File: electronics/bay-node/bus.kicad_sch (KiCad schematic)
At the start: 9 parts, among them U11 TCAN1044AV

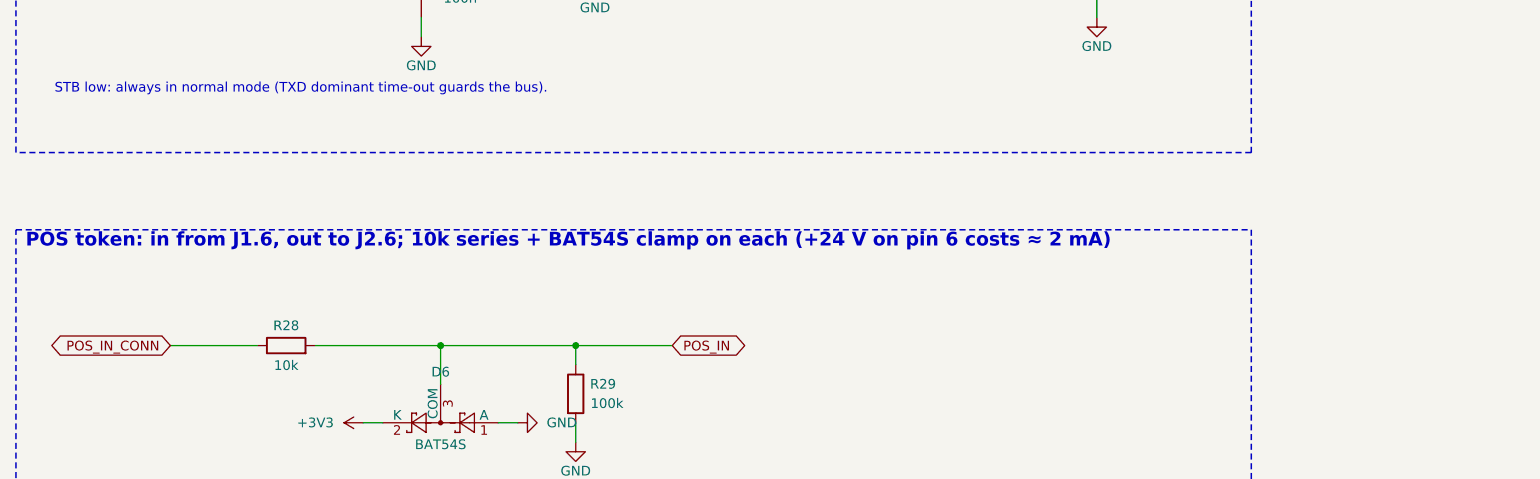
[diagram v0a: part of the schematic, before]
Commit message: Bay node v0.5: VRACK, GCT USB-C, VBUS caps on the ESD parts
Follows the power box's switch to USB-C PD (docs/can.md on the power-box branch):

- Pin 1 of the row cable is VRACK (20 V, or 28 V EPR): the net 24V_BUS becomes
  VRACK and +24V (after the P-FET) becomes VIN, in the schematic, the zones and
  the netclass patterns.  The input stage already takes 20-28 V.
- J3/J4 become the GCT USB4105-GF-A-120 (catalog usbc5a, LCSC C5184243), the
  part the user approved for the hub.  KiCad 10 ships its 3D model.  The pads
  sit 0.365 mm closer to the footprint origin than the HRO's, so the hand-drawn
  USB High-Speed tracks move with them (both lines of each pair alike, so the
  matching holds).  A board rule allows the footprint's own 0.19 mm between its
  GND pads and its pegs, the same rule the hub uses.
- Konnect's open point from v0.4: C25 and C26 (100 nF) on U4's and U8's VBUS.
- JLC_CPL_FIX: C5184243 at 0 deg, -1.30 mm y (EasyEDA fit, residual 0).
- JLC_SINCE_QUOTE: +$2.38 of parts per board ($38.10 for the 16 quoted).

ERC 0, DRC 0, unconnected 0, parity 0; Konnect's design review shows only the
known per-sheet false positives.  CAN stubs to U11: 2.2 / 7.9 mm.

Co-Authored-By: Claude Opus 5.5 <noreply@anthropic.com>
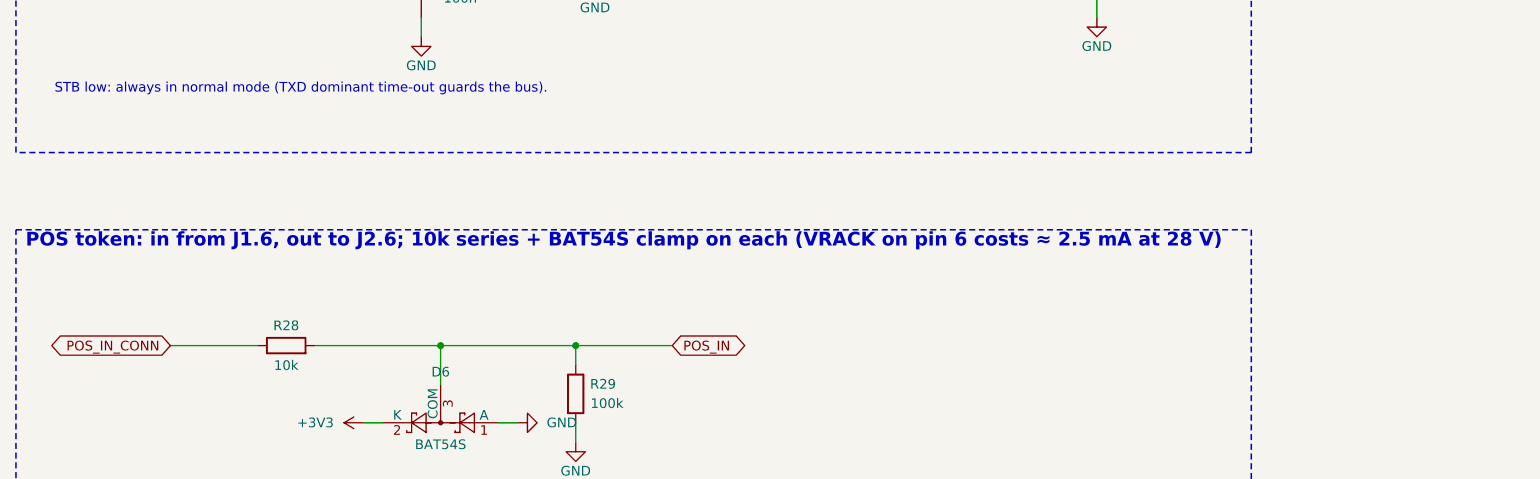
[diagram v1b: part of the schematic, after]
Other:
- note added: "POS token: in from J1.6, out to J2.6; 10k series + BAT54S clamp on each (VRACK on pin 6 costs ≈ 2.5 mA at 28 V)"
- note removed: "POS token: in from J1.6, out to J2.6; 10k series + BAT54S clamp on each (+24 V on pin 6 costs ≈ 2 mA)"
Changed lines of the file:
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@@
 		)
 	)
-	(text "POS token: in from J1.6, out to J2.6; 10k series + BAT54S clamp on each (+24 V on pin 6 costs ≈ 2 mA)"
+	(text "POS token: in from J1.6, out to J2.6; 10k series + BAT54S clamp on each (VRACK on pin 6 costs ≈ 2.5 mA at 28 V)"
 		(exclude_from_sim no)
 		(at 16.51 93.98 0)

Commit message: CAN transceiver: TCAN1462V (signal improvement) on the hub and the bay node
Same SOIC-8 pinout as the TCAN1044AV (VIO on pin 5, STB on pin 8), so the
footprint, placement and routing are unchanged: the regenerated PCBs keep
every track and via, only U6 / U11's value and fields change.  Signal
improvement (CiA 601-4, ISO 11898-2:2024 set C) damps the ringing of the
star's open branch ends; the termination (56 ohm at the hub) stays.

* catalog: TCAN1462VDRQ1 (C7399456, no LCSC stock on 2026-10-18), with the
  TCAN1044AVDRQ1 (C3234993) and NXP TJA1462AT/0Z (C3234095) as alternates;
  CPL rotation for all three.
* BOM: the board BOMs' alternates now show in the rack BOM notes; JLC
  estimates +$0.54 per board.
* docs/can.md: why the star is fine at 250 kbit/s and what SIC adds, with
  sources (TI SLLSFF2B, SLLA581A; CiA bit-timing table; NXP TJA1462).
* Both boards: ERC 0, DRC 0 errors, 0 unconnected, parity 0; 3D 0 stand-ins.

Co-Authored-By: Claude Opus 5.5 <noreply@anthropic.com>
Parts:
- U11: value TCAN1044AV -> TCAN1462V; Alternative (none) -> LCSC stock was 0 on 2026-10-18. Same pinout: TCAN1044AVDRQ1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; LCSC C3234993 -> C7399456; MPN TCAN1044AVDRQ1 -> TCAN1462VDRQ1
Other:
- note added: "CAN: TCAN1462V on the row pair (J1.3/4 ↔ J2.3/4, Power sheet); stub ≤ 20 mm, no termination"
- note removed: "CAN: TCAN1044AV on the row pair (J1.3/4 ↔ J2.3/4, Power sheet); stub ≤ 20 mm, no termination"
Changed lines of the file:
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@@
 			)
 		)
-		(property "Value" "TCAN1044AV"
-			(at 86.53 34.29 0)
+		(property "Value" "TCAN1462V"
+			(at 86.005 34.29 0)
 			(effects
 				(font
@@
 			)
 		)
-		(property "Datasheet" "https://www.ti.com/lit/ds/symlink/tcan1044av-q1.pdf"
+		(property "Datasheet" "https://www.ti.com/lit/ds/symlink/tcan1462-q1.pdf"
 			(at 91.44 45.72 0)
 			(effects
@@
 			)
 		)
-		(property "Description" "CAN FD transceiver, VCC 5 V, VIO 1.8–5 V, bus pins ±58 V (MCP2562 pinout)"
+		(property "Description" "CAN FD SIC transceiver, VCC 5 V, VIO 1.7–5.5 V, bus pins ±58 V (MCP2562 pinout)"
 			(at 91.44 45.72 0)
 			(effects
@@
 			)
 		)
-		(property "MPN" "TCAN1044AVDRQ1"
+		(property "MPN" "TCAN1462VDRQ1"
 			(at 91.44 45.72 0)
 			(effects
@@
 			)
 		)
-		(property "LCSC" "C3234993"
+		(property "LCSC" "C7399456"
+			(at 91.44 45.72 0)
+			(effects
+				(font
+					(size 1.27 1.27)
+				)
+				(hide yes)
+			)
+		)
+		(property "Alternative" "LCSC stock was 0 on 2026-10-18.  Same pinout: TCAN1044AVDRQ1 (C3234993, no SIC, ±58 V) or NXP TJA1462AT/0Z (C3234095, SIC, VIO 2.95–5.5 V, bus pins −36/+40 V)"
 			(at 91.44 45.72 0)
 			(effects
@@
 		)
 	)
-	(text "CAN: TCAN1044AV on the row pair (J1.3/4 ↔ J2.3/4, Power sheet); stub ≤ 20 mm, no termination"
+	(text "CAN: TCAN1462V on the row pair (J1.3/4 ↔ J2.3/4, Power sheet); stub ≤ 20 mm, no termination"
 		(exclude_from_sim no)
 		(at 16.51 17.78 0)
@@
 		)
 	)
-	(text_box "CAN (docs/can.md): one bus for the rack, a star from the hub; both terminations sit in the hub.\n  250 kbit/s (125 kbit/s fallback).  TCAN1044AV: VCC 5 V, VIO 3.3 V, bus pins ±58 V, passive unpowered.\nPOS: active-high 3.3 V token.  From reset the node holds POS_OUT low; when POS_IN goes high and it has\n  no address yet, it answers with its MAC, takes (row, position) from the hub, then raises POS_OUT.\n  R29 keeps POS_IN low with no cable; the next node's 100k keeps POS_OUT low before firmware."
+	(text_box "CAN (docs/can.md): one bus for the rack, a star from the hub; both terminations sit in the hub.\n  250 kbit/s (125 kbit/s fallback).  TCAN1462V (SIC): VCC 5 V, VIO 3.3 V, bus pins ±58 V, passive unpowered.\nPOS: active-high 3.3 V token.  From reset the node holds POS_OUT low; when POS_IN goes high and it has\n  no address yet, it answers with its MAC, takes (row, position) from the hub, then raises POS_OUT.\n  R29 keeps POS_IN low with no cable; the next node's 100k keeps POS_OUT low before firmware."
 		(exclude_from_sim no)
 		(at 15.24 177.8 0)

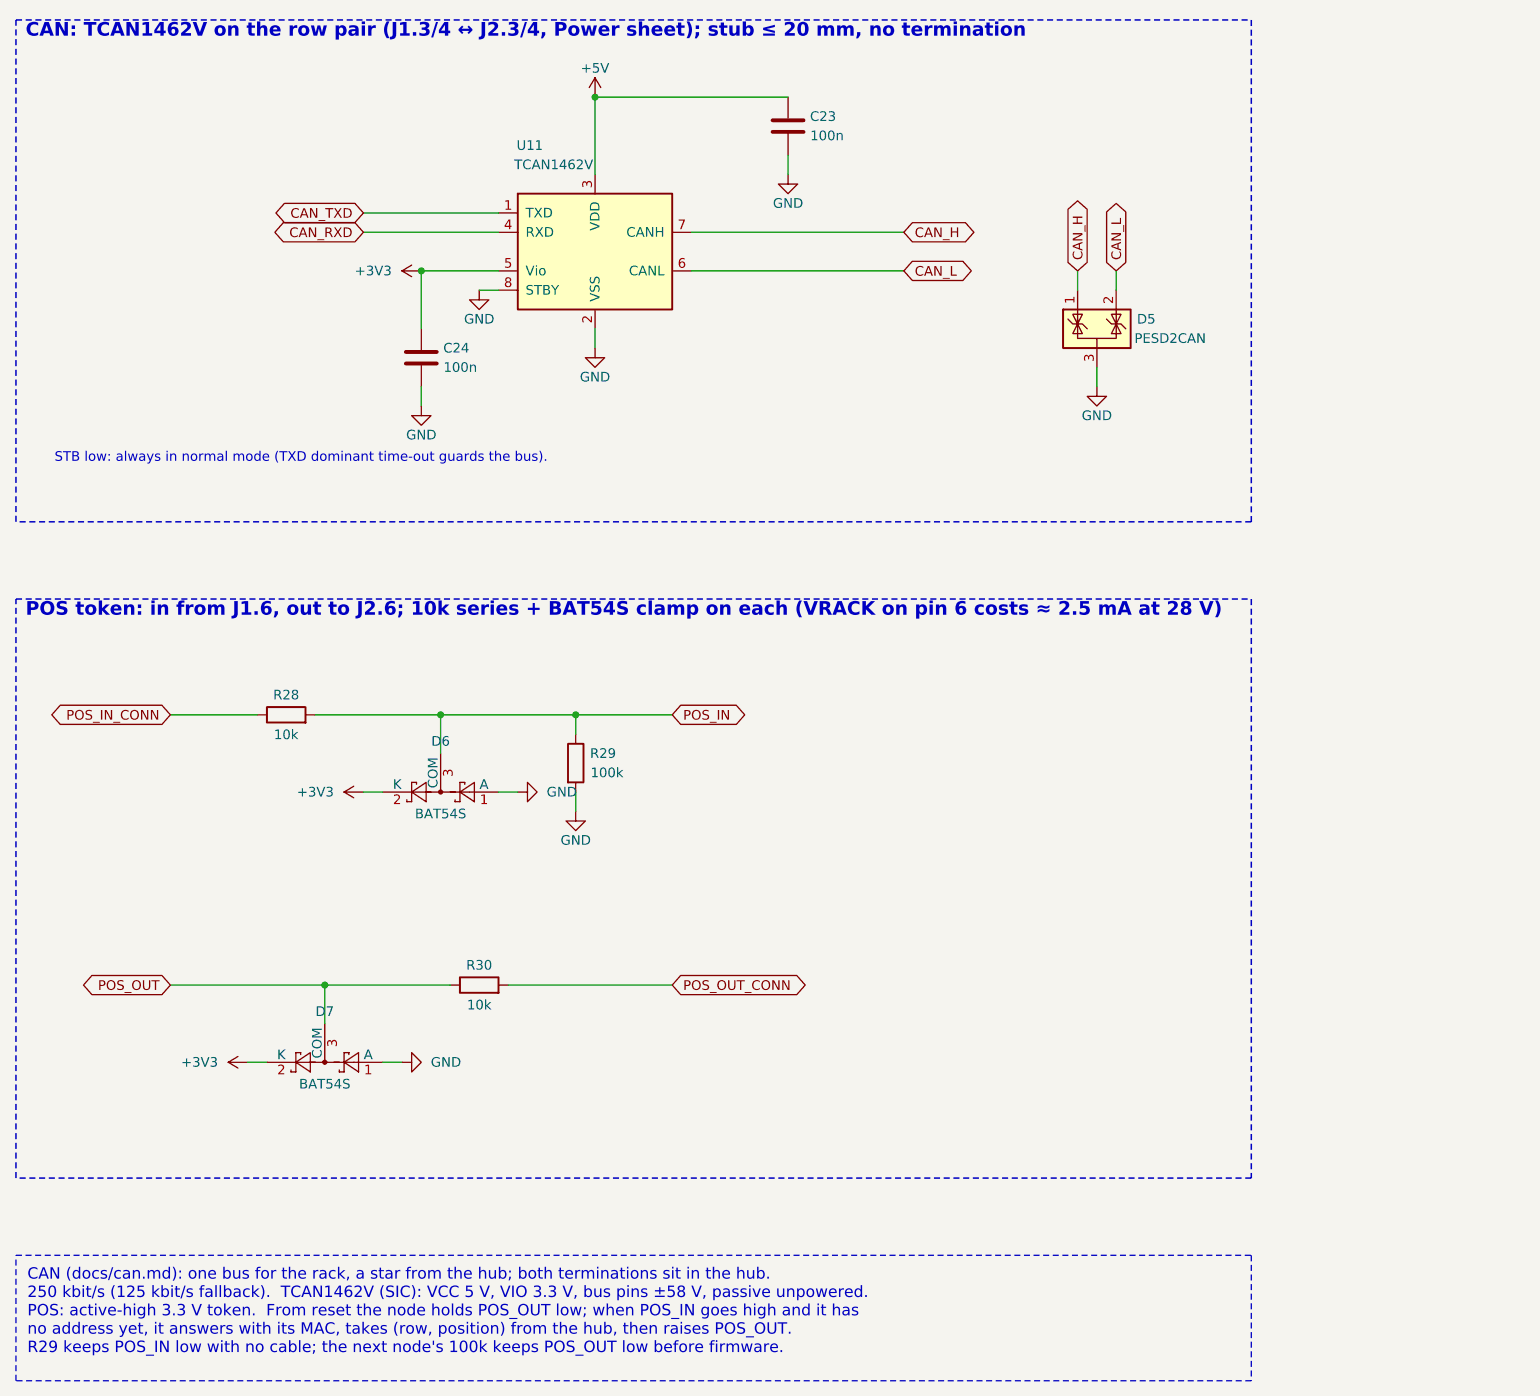
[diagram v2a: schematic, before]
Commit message: Row cable without a twist: J2 mirrored on the bay node
J1 and J2 are the same side-entry footprint turned 180°, so with one pinout
on both, the 1:1 jumper between two nodes had to make a half twist.  J2 now
carries J1's pinout mirrored (J2.n = J1.(7-n): 1 POS out, 2 GND, 3 CAN_L,
4 CAN_H, 5 GND, 6 VRACK):

* the jumper lies flat: pin n to pin 7-n, both plugs the same face up;
* every net crosses the node straight: the In2 VRACK strip runs from J1.1
  to J2.6 at the same height, and R30 sits by J2.1;
* the hub keeps J1's pinout and the feeds stay 1:1: out of the box's left
  wall and back into J1 from the left, they fold over once;
* a wrong cable burns nothing: VRACK lands on a POS pin (10k + BAT54S),
  CAN swaps, and the next node stays off.

The node is re-routed: ERC 0, DRC 0, unconnected 0, parity 0; CAN stubs
≤ 8.2 mm; 85 3D models, 0 stand-ins.  docs/can.md (the contract),
cabling.md, electronics.md, the Konnect review, the BOM cable lines and the
viewer's jumper (flat again) follow.

Co-Authored-By: Claude Opus 5.5 <noreply@anthropic.com>
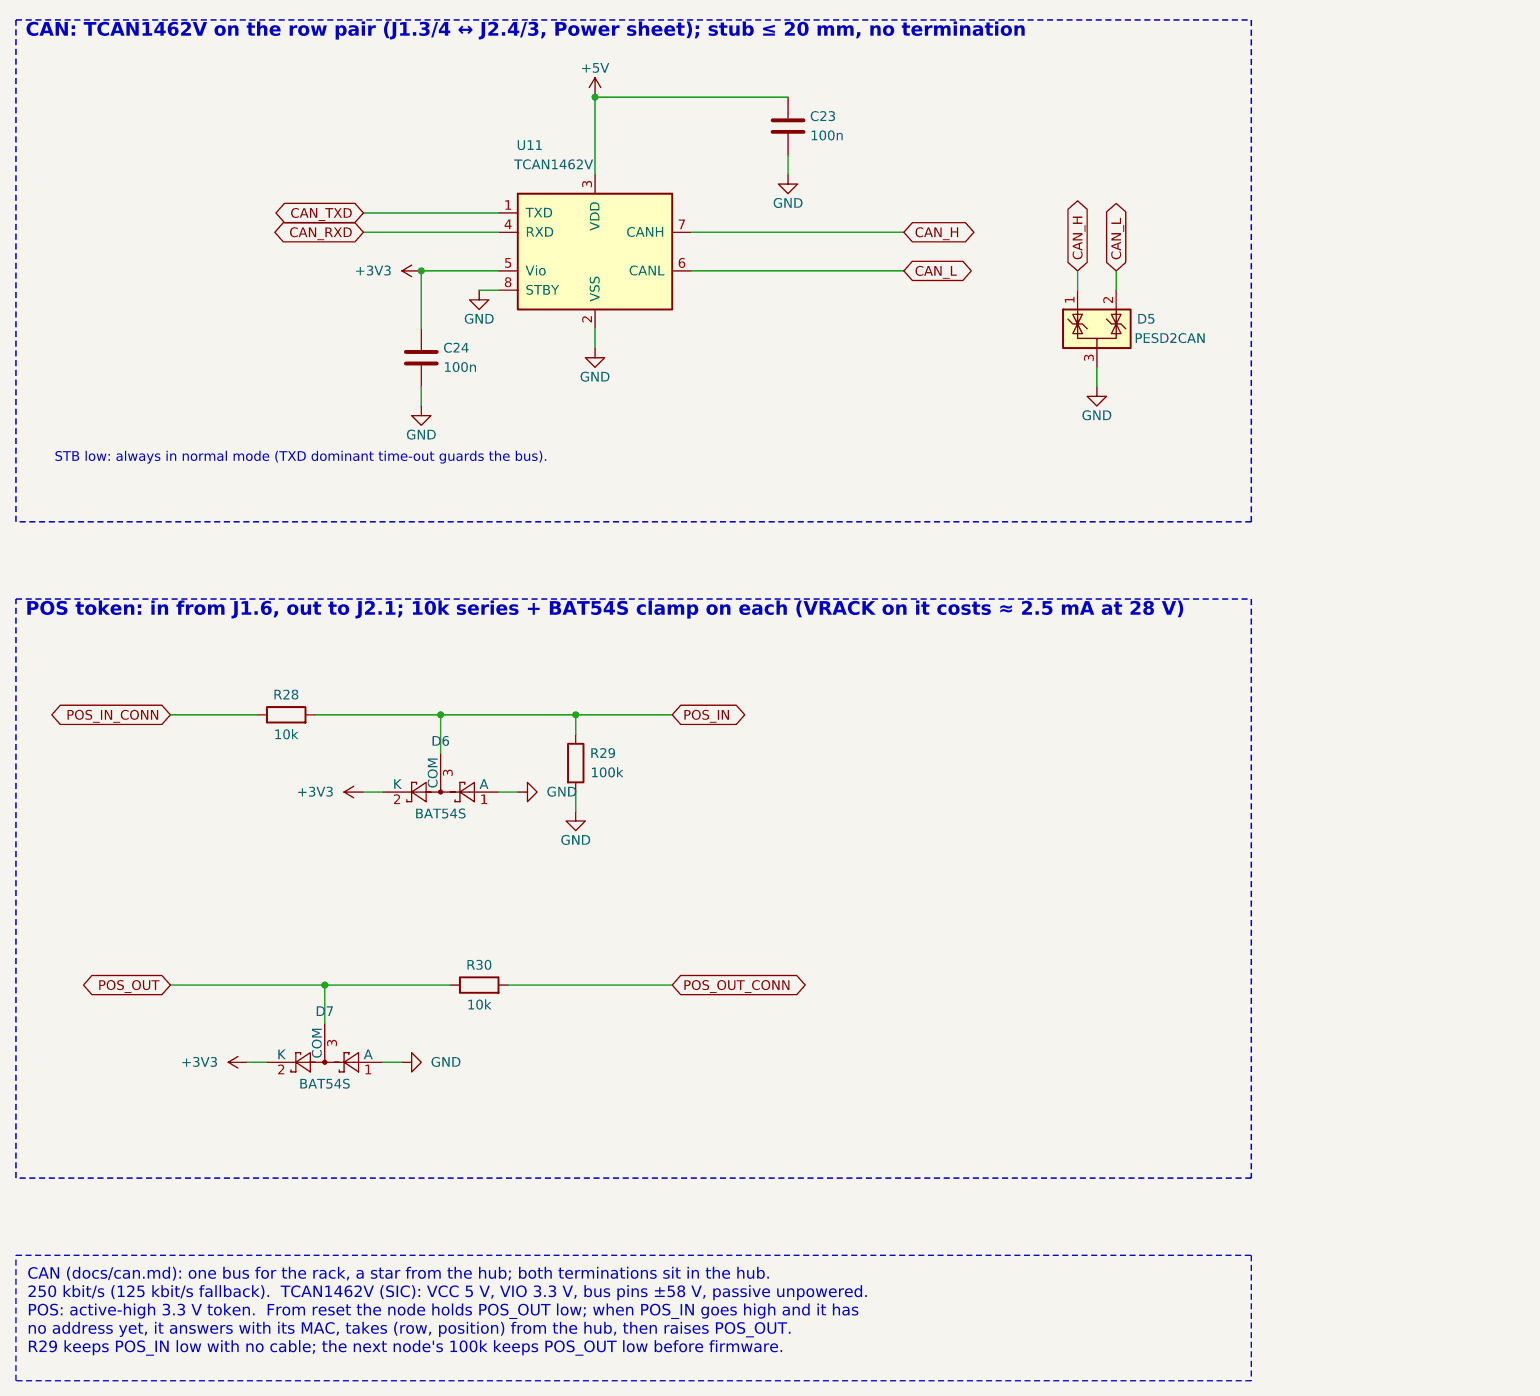
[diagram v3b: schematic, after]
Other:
- note added: "CAN: TCAN1462V on the row pair (J1.3/4 ↔ J2.4/3, Power sheet); stub ≤ 20 mm, no termination"
- note added: "POS token: in from J1.6, out to J2.1; 10k series + BAT54S clamp on each (VRACK on it costs ≈ 2.5 mA at 28 V)"
- note removed: "CAN: TCAN1462V on the row pair (J1.3/4 ↔ J2.3/4, Power sheet); stub ≤ 20 mm, no termination"
- note removed: "POS token: in from J1.6, out to J2.6; 10k series + BAT54S clamp on each (VRACK on pin 6 costs ≈ 2.5 mA at 28 V)"
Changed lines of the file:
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@@
 		)
 	)
-	(text "CAN: TCAN1462V on the row pair (J1.3/4 ↔ J2.3/4, Power sheet); stub ≤ 20 mm, no termination"
+	(text "CAN: TCAN1462V on the row pair (J1.3/4 ↔ J2.4/3, Power sheet); stub ≤ 20 mm, no termination"
 		(exclude_from_sim no)
 		(at 16.51 17.78 0)
@@
 		)
 	)
-	(text "POS token: in from J1.6, out to J2.6; 10k series + BAT54S clamp on each (VRACK on pin 6 costs ≈ 2.5 mA at 28 V)"
+	(text "POS token: in from J1.6, out to J2.1; 10k series + BAT54S clamp on each (VRACK on it costs ≈ 2.5 mA at 28 V)"
 		(exclude_from_sim no)
 		(at 16.51 93.98 0)
